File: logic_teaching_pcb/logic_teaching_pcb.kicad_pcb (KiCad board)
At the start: 2 copper layers, 200 x 180 mm, 107 parts, among them J1 Conn_01x02, J10 Conn_01x02, J11 Conn_01x01, J12 Conn_01x02, J13 Conn_01x02, J14 Conn_01x01, J15 Conn_01x02, J16 Conn_01x01, J17 Conn_01x01, J18 Conn_01x01, J19 Conn_01x01, J2 Conn_01x02, J20 Conn_01x01, J21 Conn_01x01, J22 Conn_01x01, J23 Conn_01x01, J24 Conn_01x01, J25 Conn_01x02, J26 Conn_01x01, J27 Conn_01x02, J28 Conn_01x01, J29 Conn_01x02, J3 Conn_01x02, J30 Conn_01x02, J31 Conn_01x02, J32 Conn_01x01, J33 Conn_01x02, J34 Conn_01x01, J35 Conn_01x02, J36 Conn_01x01, J37 Conn_01x02, J38 Conn_01x01, J39 Conn_01x02, J4 Conn_01x02, J40 Conn_01x01, J41 Conn_01x02, J42 Conn_01x01, J43 Conn_01x02, J44 Conn_01x01, J45 Conn_01x01, J46 Conn_01x02, J47 Conn_01x01, J48 Conn_01x02, J49 Conn_01x01, J5 Conn_01x01, J50 Conn_01x02, J51 Conn_01x01, J52 Conn_01x02, J53 Conn_01x01, J54 Conn_01x02, J55 Conn_01x01, J56 Conn_01x01, J57 Conn_01x01, J58 Conn_01x01, J59 Conn_01x02, J6 Conn_01x01, J60 Conn_01x02, J61 Conn_01x02, J62 Conn_01x02, J63 Conn_01x01, J64 Conn_01x01, J65 Conn_01x01, J66 Conn_01x01, J67 Conn_01x01, J68 Conn_01x01, J69 Conn_01x01, J7 Conn_01x01, J70 Conn_01x01, J8 Conn_01x01, J9 Conn_01x01, SW1 SW_SPDT, SW2 SW_SPDT, SW3 SW_SPDT, SW4 SW_SPDT, SW5 SW_Push, SW6 SW_Push, SW7 SW_Push, SW8 SW_Push, SW9 SW_SPDT, U1 74HC00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

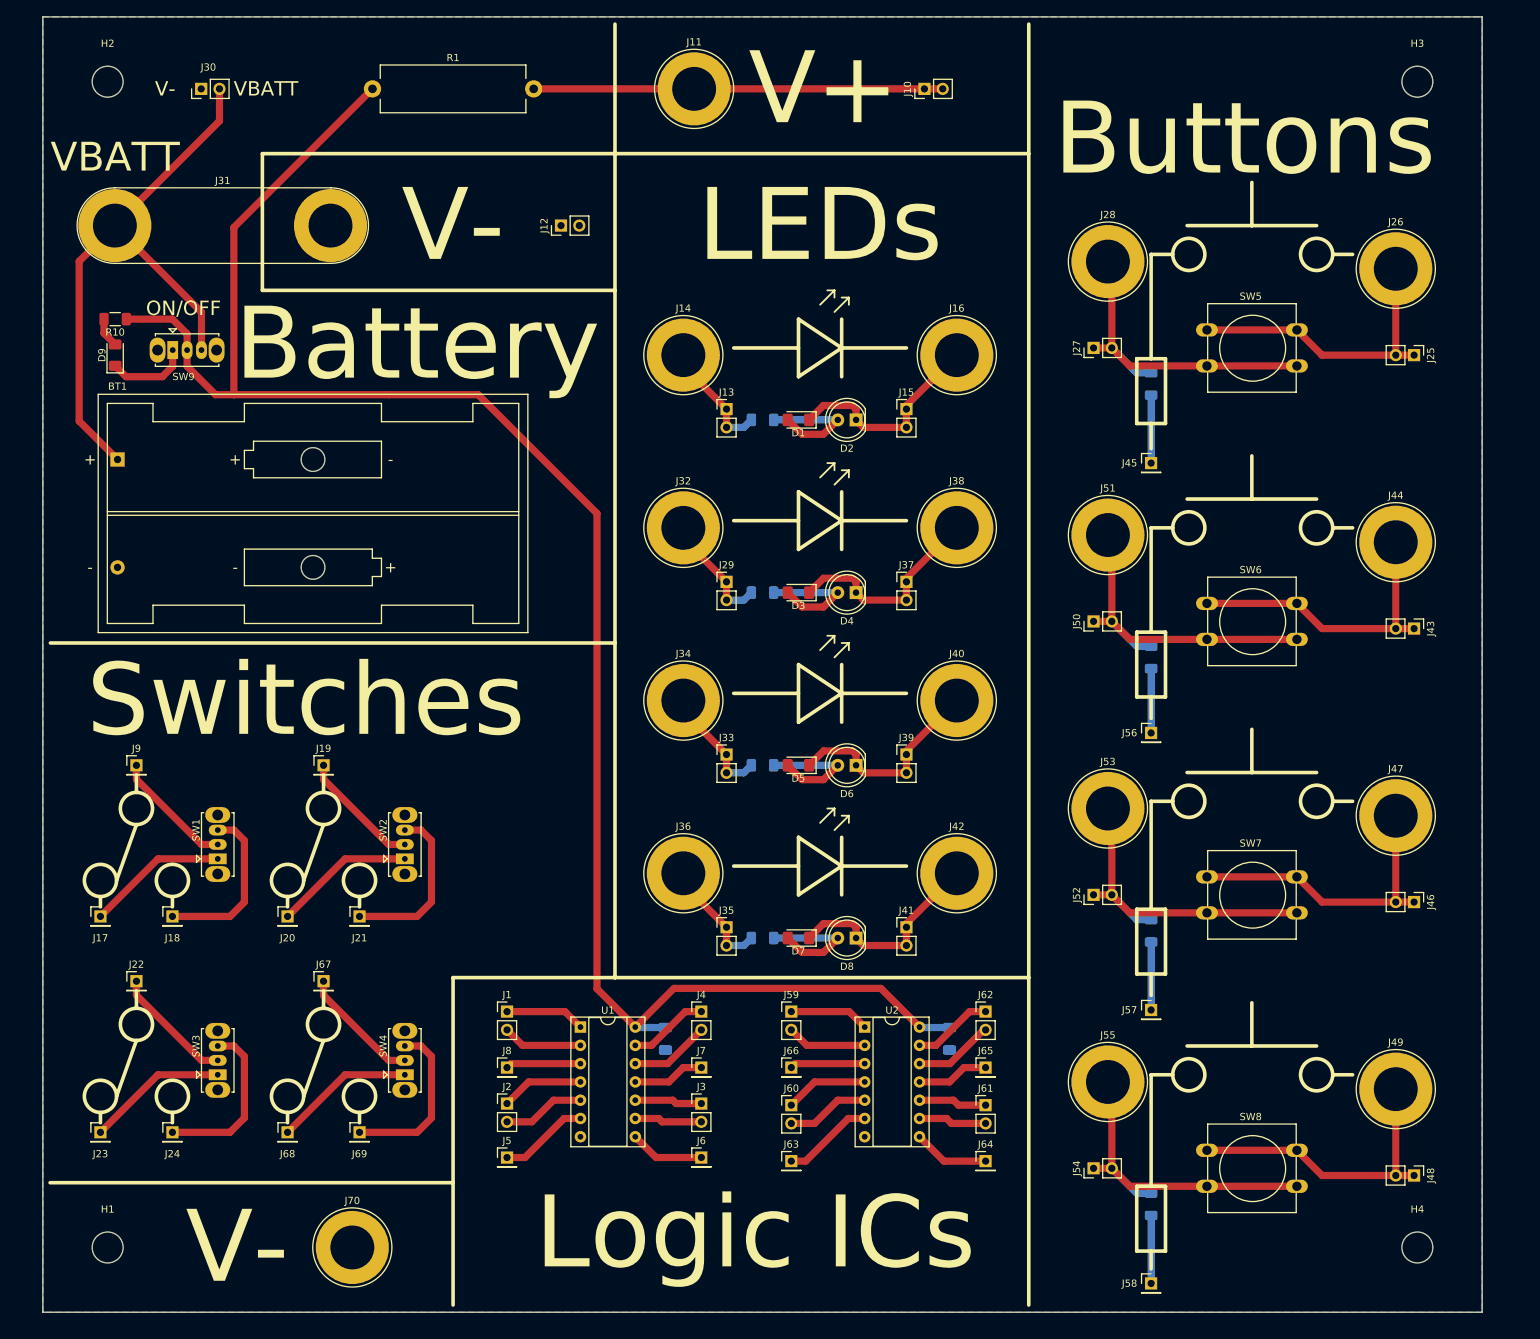
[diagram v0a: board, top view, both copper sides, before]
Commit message: change footprint to binding post, add to switches
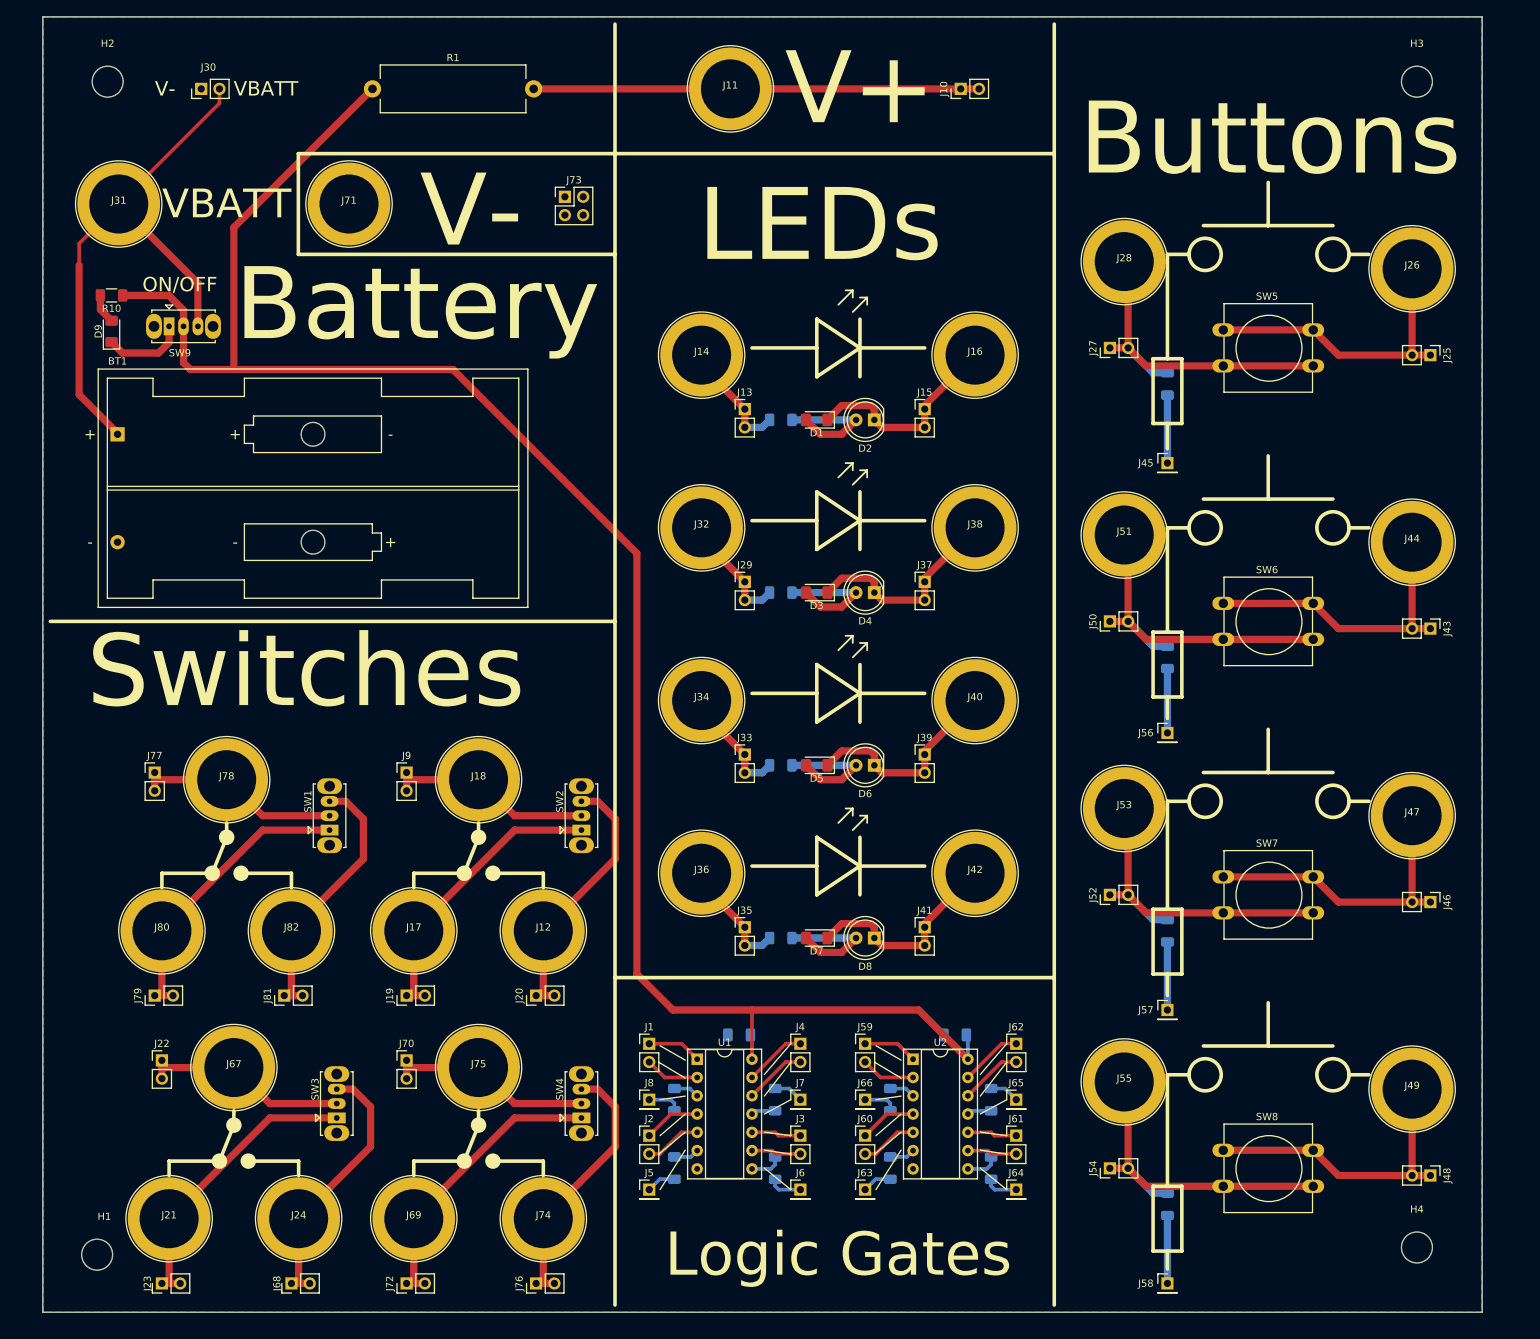
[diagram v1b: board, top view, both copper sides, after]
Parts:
- added J71: Conn_01x01, Library:BindingPost_Shin_Chin_R1-9, F.Cu at (85.0, 268.0)
- added J72: Conn_01x02, Connector_PinHeader_2.54mm:PinHeader_1x02_P2.54mm_Vertical, F.Cu at (93.0, 418.0)
- added J73: Conn_01x04, Connector_PinHeader_2.54mm:PinHeader_2x02_P2.54mm_Vertical, F.Cu at (115.0, 267.0)
- added J74: Conn_01x01, Library:BindingPost_Shin_Chin_R1-9, F.Cu at (112.0, 409.0)
- added J75: Conn_01x01, Library:BindingPost_Shin_Chin_R1-9, F.Cu at (103.0, 388.0)
- added J76: Conn_01x02, Connector_PinHeader_2.54mm:PinHeader_1x02_P2.54mm_Vertical, F.Cu at (111.0, 418.0)
- added J77: Conn_01x02, Connector_PinHeader_2.54mm:PinHeader_1x02_P2.54mm_Vertical, F.Cu at (58.0, 347.0)
- added J78: Conn_01x01, Library:BindingPost_Shin_Chin_R1-9, F.Cu at (68.0, 348.0)
- added J79: Conn_01x02, Connector_PinHeader_2.54mm:PinHeader_1x02_P2.54mm_Vertical, F.Cu at (58.0, 378.0)
- added J80: Conn_01x01, Library:BindingPost_Shin_Chin_R1-9, F.Cu at (59.0, 369.0)
- added J81: Conn_01x02, Connector_PinHeader_2.54mm:PinHeader_1x02_P2.54mm_Vertical, F.Cu at (76.0, 378.0)
- added J82: Conn_01x01, Library:BindingPost_Shin_Chin_R1-9, F.Cu at (77.0, 369.0)
- added R11: 200, Resistor_SMD:R_1206_3216Metric_Pad1.30x1.75mm_HandSolder, B.Cu at (130.2, 392.5)
- added R12: 200, Resistor_SMD:R_1206_3216Metric_Pad1.30x1.75mm_HandSolder, B.Cu at (130.2, 402.0)
- added R13: 200, Resistor_SMD:R_1206_3216Metric_Pad1.30x1.75mm_HandSolder, B.Cu at (144.2, 402.0)
- added R14: 200, Resistor_SMD:R_1206_3216Metric_Pad1.30x1.75mm_HandSolder, B.Cu at (144.2, 392.5)
- added R15: 200, Resistor_SMD:R_1206_3216Metric_Pad1.30x1.75mm_HandSolder, B.Cu at (160.2, 392.5)
- added R16: 200, Resistor_SMD:R_1206_3216Metric_Pad1.30x1.75mm_HandSolder, B.Cu at (160.2, 402.0)
- added R17: 200, Resistor_SMD:R_1206_3216Metric_Pad1.30x1.75mm_HandSolder, B.Cu at (174.2, 402.0)
- added R18: 200, Resistor_SMD:R_1206_3216Metric_Pad1.30x1.75mm_HandSolder, B.Cu at (174.2, 392.5)
- J11, J14, J16, J26, J28, J32, J34, J36, J38, J40, J42, J44, J47, J49, J51, J53, J55: footprint Connector:Banana_Jack_1Pin -> Library:BindingPost_Shin_Chin_R1-9
- J12: value Conn_01x02 -> Conn_01x01; footprint Connector_PinHeader_2.54mm:PinHeader_1x02_P2.54mm_Vertical -> Library:BindingPost_Shin_Chin_R1-9
- J17, J18, J21, J24, J67, J69: footprint Connector_PinHeader_2.54mm:PinHeader_1x01_P2.54mm_Vertical -> Library:BindingPost_Shin_Chin_R1-9
- J19, J20, J22, J23, J68, J9: value Conn_01x01 -> Conn_01x02; footprint Connector_PinHeader_2.54mm:PinHeader_1x01_P2.54mm_Vertical -> Connector_PinHeader_2.54mm:PinHeader_1x02_P2.54mm_Vertical
- J31: value Conn_01x02 -> Conn_01x01; footprint Connector:Banana_Jack_2Pin -> Library:BindingPost_Shin_Chin_R1-9
- J70: value Conn_01x01 -> Conn_01x02; footprint Connector:Banana_Jack_1Pin -> Connector_PinHeader_2.54mm:PinHeader_1x02_P2.54mm_Vertical
- moved J12 98.0 mm to (112.0, 369.0), turned to 0 degrees
- moved J21 49.6 mm to (60.0, 409.0)
- moved J18 46.6 mm to (103.0, 348.0)
- moved J17 43.6 mm to (94.0, 369.0)
- moved J9 37.6 mm to (93.0, 347.0)
- moved J20 36.2 mm to (111.0, 378.0), turned to 90 degrees
- moved J19 34.0 mm to (93.0, 378.0), turned to 90 degrees
- moved J70 27.1 mm to (93.0, 387.0)
- moved SW4 25.3 mm to (117.3, 395.0)
- moved SW2 24.9 mm to (117.3, 355.0)
- moved J23 22.7 mm to (59.0, 418.0), turned to 90 degrees
- moved J24 21.3 mm to (78.0, 409.0)
- moved J68 21.0 mm to (77.0, 418.0), turned to 90 degrees
- moved J1 20.3 mm to (126.7, 384.7)
- moved J2 20.3 mm to (126.7, 397.5)
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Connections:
- J12 pad 1: GND -> Net-(J12-Pad1)
- J19 pad 1: Net-(J19-Pad1) -> Net-(J17-Pad1)
- J20 pad 1: Net-(J20-Pad1) -> Net-(J12-Pad1)
- J23 pad 1: Net-(J23-Pad1) -> Net-(J21-Pad1)
- J67 pad 1: Net-(J67-Pad1) -> Net-(J22-Pad1)
- J68 pad 1: Net-(J68-Pad1) -> Net-(J24-Pad1)
- J70 pad 1: GND -> Net-(J70-Pad1)
- J9 pad 1: Net-(J9-Pad1) -> Net-(J18-Pad1)
- SW1 pad 1: Net-(J17-Pad1) -> Net-(SW1-Pad1)
- SW1 pad 2: Net-(J9-Pad1) -> Net-(SW1-Pad2)
- SW1 pad 3: Net-(J18-Pad1) -> Net-(SW1-Pad3)
- SW2 pad 1: Net-(J20-Pad1) -> Net-(J17-Pad1)
- SW2 pad 2: Net-(J19-Pad1) -> Net-(J18-Pad1)
- SW2 pad 3: Net-(J21-Pad1) -> Net-(J12-Pad1)
- SW3 pad 1: Net-(J23-Pad1) -> Net-(J21-Pad1)
- SW4 pad 1: Net-(J68-Pad1) -> Net-(J69-Pad1)
- SW4 pad 2: Net-(J67-Pad1) -> Net-(J70-Pad1)
- SW4 pad 3: Net-(J69-Pad1) -> Net-(J74-Pad1)
- U1 pad 11: Net-(J7-Pad1) -> Net-(U1-Pad11)
- U1 pad 3: Net-(J8-Pad1) -> Net-(U1-Pad3)
- U1 pad 6: Net-(J5-Pad1) -> Net-(U1-Pad6)
- U1 pad 8: Net-(J6-Pad1) -> Net-(U1-Pad8)
- U2 pad 11: Net-(J65-Pad1) -> Net-(U2-Pad11)
- U2 pad 3: Net-(J66-Pad1) -> Net-(U2-Pad3)
- U2 pad 6: Net-(J63-Pad1) -> Net-(U2-Pad6)
- U2 pad 8: Net-(J64-Pad1) -> Net-(U2-Pad8)
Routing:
- net Net-(SW1-Pad1): track 0.00 -> 40.6 mm
- net Net-(SW1-Pad3): track 0.00 -> 36.9 mm
- net Net-(J74-Pad1): track 0.00 -> 36.9 mm
- net Net-(J12-Pad1): track 0.00 -> 36.9 mm
- net Net-(SW1-Pad2): track 0.00 -> 28.9 mm
- net Net-(J70-Pad1): track 0.00 -> 28.9 mm
- net Net-(J17-Pad1): track 19.6 -> 40.6 mm
- net Net-(J68-Pad1): track 19.6 -> 0.00 mm
- net Net-(J20-Pad1): track 19.6 -> 0.00 mm
- net Net-(J23-Pad1): track 19.6 -> 0.00 mm
- net Net-(J67-Pad1): track 17.0 -> 0.00 mm
- net Net-(J19-Pad1): track 17.0 -> 0.00 mm
- net Net-(J9-Pad1): track 17.0 -> 0.00 mm
- net Net-(J69-Pad1): track 23.7 -> 40.6 mm
- net Net-(J21-Pad1): track 23.7 -> 40.6 mm
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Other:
- board text added: "Logic Gates"
- board text removed: "Logic ICs"
